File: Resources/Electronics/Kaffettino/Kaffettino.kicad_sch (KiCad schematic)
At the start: 52 parts, among them J1 PPTC101LFBN-RC, J2 OSTVN02A150, J3 OSTVN04A150, J5 OSTVN04A150, M1 RFID-RC522, U1 PCF8574AN, U2 ESP32-38Pin-Wroom, U3 DFR0299

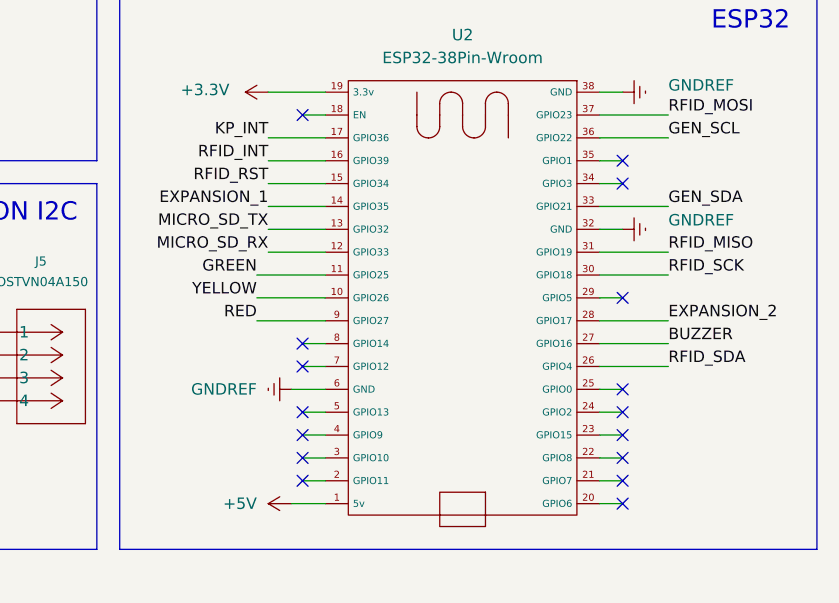
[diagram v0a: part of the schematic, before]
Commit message: NFC Reader interrupt
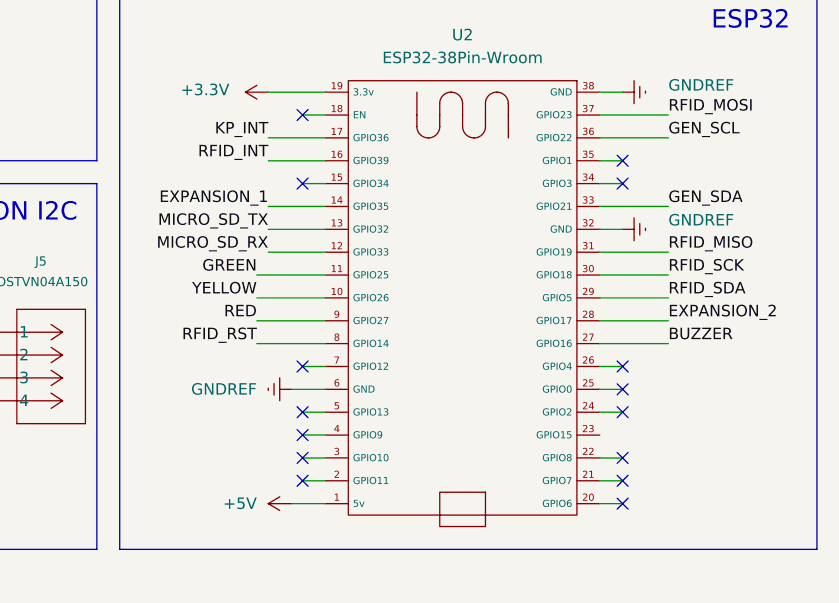
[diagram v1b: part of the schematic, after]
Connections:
- net RFID_RST: now also U2.8 (GPIO14); no longer U2.15 (GPIO34)
- net RFID_SDA: now also U2.29 (GPIO5); no longer U2.26 (GPIO4)
- no-connect marks 27 -> 26
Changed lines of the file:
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@@
+	)
+	(no_connect
+		(at 261.62 143.51)
 	)
 	(no_connect
@@
 	)
 	(no_connect
+		(at 226.06 123.19)
+	)
+	(no_connect
 		(at 219.71 67.31)
 	)
@@
 	)
 	(no_connect
-		(at 261.62 151.13)
-	)
-	(no_connect
 		(at 226.06 153.67)
 	)
@@
 	)
 	(no_connect
-		(at 226.06 140.97)
-	)
-	(no_connect
-		(at 261.62 135.89)
-	)
-	(no_connect
 		(at 226.06 156.21)
 	)
@@
 	(wire
 		(pts
-			(xy 226.06 140.97) (xy 228.6 140.97)
-		)
-		(stroke
-			(width 0)
-			(type default)
-		)
-	)
-	(wire
-		(pts
 			(xy 259.08 113.03) (xy 261.62 113.03)
 		)
@@
 	(wire
 		(pts
+			(xy 220.98 140.97) (xy 228.6 140.97)
+		)
+		(stroke
+			(width 0)
+			(type default)
+		)
+	)
+	(wire
+		(pts
 			(xy 226.06 151.13) (xy 228.6 151.13)
 		)
@@
 	(wire
 		(pts
-			(xy 261.62 135.89) (xy 259.08 135.89)
-		)
-		(stroke
-			(width 0)
-			(type default)
-		)
-	)
-	(wire
-		(pts
 			(xy 186.69 144.78) (xy 189.23 144.78)
 		)
@@
 	(wire
 		(pts
+			(xy 261.62 143.51) (xy 259.08 143.51)
+		)
+		(stroke
+			(width 0)
+			(type default)
+		)
+	)
+	(wire
+		(pts
 			(xy 77.47 20.32) (xy 82.55 20.32)
 		)
@@
 	(wire
 		(pts
+			(xy 259.08 135.89) (xy 266.7 135.89)
+		)
+		(stroke
+			(width 0)
+			(type default)
+		)
+	)
+	(wire
+		(pts
 			(xy 259.08 128.27) (xy 261.62 128.27)
 		)
@@
 	(wire
 		(pts
+			(xy 226.06 123.19) (xy 228.6 123.19)
+		)
+		(stroke
+			(width 0)
+			(type default)
+		)
+	)
+	(wire
+		(pts
 			(xy 143.51 157.48) (xy 143.51 162.56)
 		)
@@
 	(wire
 		(pts
-			(xy 259.08 143.51) (xy 266.7 143.51)
-		)
-		(stroke
-			(width 0)
-			(type default)
-		)
-	)
-	(wire
-		(pts
 			(xy 77.47 43.18) (xy 82.55 43.18)
 		)
@@
 	(wire
 		(pts
-			(xy 222.25 123.19) (xy 228.6 123.19)
-		)
-		(stroke
-			(width 0)
-			(type default)
-		)
-	)
-	(wire
-		(pts
 			(xy 115.57 27.94) (xy 115.57 33.02)
 		)
@@
 		(pts
 			(xy 95.25 114.3) (xy 95.25 71.12)
-		)
-		(stroke
-			(width 0)
-			(type default)
-		)
-	)
-	(wire
-		(pts
-			(xy 261.62 151.13) (xy 259.08 151.13)
 		)
 		(stroke
@@
 		)
 	)
+	(label "RFID_SDA"
+		(at 266.7 135.89 0)
+		(effects
+			(font
+				(size 1.27 1.27)
+			)
+			(justify left bottom)
+		)
+	)
 	(label "KP_R2"
 		(at 129.54 20.32 0)
@@
 		)
 	)
-	(label "RFID_SDA"
-		(at 266.7 143.51 0)
-		(effects
-			(font
-				(size 1.27 1.27)
-			)
-			(justify left bottom)
-		)
-	)
 	(label "KP_C2"
 		(at 129.54 71.12 0)
@@
 		)
 	)
-	(label "RFID_RST"
-		(at 222.25 123.19 180)
-		(effects
-			(font
-				(size 1.27 1.27)
-			)
-			(justify right bottom)
-		)
-	)
 	(label "MICRO_SD_TX"
 		(at 266.7 69.85 0)
@@
 		)
 	)
+	(label "RFID_RST"
+		(at 220.98 140.97 180)
+		(effects
+			(font
+				(size 1.27 1.27)
+			)
+			(justify right bottom)
+		)
+	)

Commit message: Working mp3 player, oled screen and nfc scanner
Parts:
- R24: now fitted
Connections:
- net BUZZER: now also U2.12 (GPIO33); no longer U2.27 (GPIO16)
- net EXPANSION_2: now also U2.13 (GPIO32); no longer U2.28 (GPIO17)
- net MICRO_SD_RX: now also U2.27 (GPIO16); no longer U2.12 (GPIO33)
- net MICRO_SD_TX: now also U2.28 (GPIO17); no longer U2.13 (GPIO32)
- no-connect marks 26 -> 27
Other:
- note added: "Can be used"
- note added: "MP3 PLAYER"
- note added: "NFC READER"
- note added: "OLED DISPLAY"
- note added: "STATUS LED"
- note added: "We should remember that we cannot use: - 34, 35, 36, 39: Are only input pins without an internal resistor - 6, 7, 8, 9, 10, 11: Flash memory, do not use - 0, 2: Strapping pin (booting the esp32) - 1, 3: Serial line for debugging - 4, 12, 13, 14, 25, 26, 27: Only digital reads and writes work with wifi"
- note removed: "DISPLAY OLED"
- note removed: "LED DI STATO"
- note removed: "LETTORE NFC"
- note removed: "LETTORE SD"
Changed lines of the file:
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@@
 		)
 	)
-	(text "LED DI STATO"
+	(text "STATUS LED"
 		(exclude_from_sim no)
 		(at 60.706 150.622 0)
@@
 		)
 	)
-	(text "LETTORE NFC\n"
+	(text "NFC READER\n"
 		(exclude_from_sim no)
 		(at 272.034 17.018 0)
@@
 		)
 	)
-	(text "DISPLAY OLED\n"
+	(text "Can be used"
+		(exclude_from_sim no)
+		(at 264.414 151.384 0)
+		(effects
+			(font
+				(size 1.27 1.27)
+			)
+			(justify left)
+		)
+	)
+	(text "Can be used"
+		(exclude_from_sim no)
+		(at 208.534 122.682 0)
+		(effects
+			(font
+				(size 1.27 1.27)
+			)
+			(justify left)
+		)
+	)
+	(text "We should remember that we cannot use:\n- 34, 35, 36, 39: Are only input pins without an internal resistor\n- 6, 7, 8, 9, 10, 11: Flash memory, do not use\n- 0, 2: Strapping pin (booting the esp32)\n- 1, 3: Serial line for debugging\n- 4, 12, 13, 14, 25, 26, 27: Only digital reads and writes work with wifi"
+		(exclude_from_sim no)
+		(at 302.006 126.746 0)
+		(effects
+			(font
+				(size 1.27 1.27)
+			)
+			(justify left)
+		)
+	)
+	(text "OLED DISPLAY"
 		(exclude_from_sim no)
 		(at 42.418 126.238 0)
@@
 		)
 	)
-	(text "LETTORE SD\n"
+	(text "MP3 PLAYER\n"
 		(exclude_from_sim no)
 		(at 271.78 51.816 0)
@@
 	)
 	(no_connect
-		(at 261.62 123.19)
-	)
-	(no_connect
-		(at 261.62 146.05)
+		(at 226.06 123.19)
 	)
 	(no_connect
-		(at 261.62 156.21)
+		(at 226.06 143.51)
 	)
 	(no_connect
-		(at 261.62 153.67)
+		(at 261.62 123.19)
 	)
 	(no_connect
-		(at 226.06 115.57)
+		(at 261.62 158.75)
 	)
 	(no_connect
@@
 	)
 	(no_connect
-		(at 261.62 143.51)
+		(at 261.62 151.13)
 	)
 	(no_connect
@@
 	)
 	(no_connect
-		(at 33.02 25.4)
+		(at 261.62 153.67)
 	)
 	(no_connect
-		(at 226.06 123.19)
+		(at 33.02 25.4)
 	)
 	(no_connect
@@
 	)
 	(no_connect
-		(at 226.06 143.51)
+		(at 261.62 120.65)
 	)
 	(no_connect
-		(at 226.06 151.13)
+		(at 261.62 156.21)
 	)
 	(no_connect
-		(at 261.62 148.59)
+		(at 226.06 151.13)
 	)
 	(no_connect
-		(at 226.06 153.67)
+		(at 226.06 115.57)
 	)
 	(no_connect
@@
 	)
 	(no_connect
-		(at 261.62 158.75)
+		(at 261.62 143.51)
 	)
 	(no_connect
-		(at 226.06 156.21)
+		(at 261.62 146.05)
 	)
 	(no_connect
-		(at 261.62 120.65)
+		(at 226.06 153.67)
+	)
+	(no_connect
+		(at 261.62 148.59)
+	)
+	(no_connect
+		(at 226.06 156.21)
 	)
 	(no_connect
@@
 	(wire
 		(pts
+			(xy 220.98 140.97) (xy 228.6 140.97)
+		)
+		(stroke
+			(width 0)
+			(type default)
+		)
+	)
+	(wire
+		(pts
 			(xy 115.57 101.6) (xy 115.57 106.68)
 		)
@@
 	(wire
 		(pts
-			(xy 259.08 140.97) (xy 266.7 140.97)
+			(xy 228.6 130.81) (xy 220.98 130.81)
 		)
 		(stroke
@@
 	(wire
 		(pts
-			(xy 220.98 140.97) (xy 228.6 140.97)
-		)
-		(stroke
-			(width 0)
-			(type default)
-		)
-	)
-	(wire
-		(pts
 			(xy 226.06 151.13) (xy 228.6 151.13)
 		)
@@
 	(wire
 		(pts
-			(xy 222.25 125.73) (xy 228.6 125.73)
+			(xy 220.98 125.73) (xy 228.6 125.73)
 		)
 		(stroke
@@
 	(wire
 		(pts
-			(xy 222.25 120.65) (xy 228.6 120.65)
+			(xy 220.98 120.65) (xy 228.6 120.65)
 		)
 		(stroke
@@
 	(wire
 		(pts
-			(xy 222.25 128.27) (xy 228.6 128.27)
+			(xy 265.43 138.43) (xy 259.08 138.43)
 		)
 		(stroke
@@
 	(wire
 		(pts
-			(xy 220.98 133.35) (xy 228.6 133.35)
-		)
-		(stroke
-			(width 0)
-			(type default)
-		)
-	)
-	(wire
-		(pts
 			(xy 259.08 118.11) (xy 266.7 118.11)
 		)
@@
 	(wire
 		(pts
-			(xy 222.25 130.81) (xy 228.6 130.81)
+			(xy 265.43 140.97) (xy 259.08 140.97)
 		)
 		(stroke
@@
 	(wire
 		(pts
+			(xy 220.98 135.89) (xy 228.6 135.89)
+		)
+		(stroke
+			(width 0)
+			(type default)
+		)
+	)
+	(wire
+		(pts
+			(xy 220.98 133.35) (xy 228.6 133.35)
+		)
+		(stroke
+			(width 0)
+			(type default)
+		)
+	)
+	(wire
+		(pts
 			(xy 157.48 104.14) (xy 160.02 104.14)
 		)
@@
 	(wire
 		(pts
-			(xy 255.27 64.77) (xy 252.73 64.77)
+			(xy 261.62 151.13) (xy 259.08 151.13)
 		)
 		(stroke
@@
 	(wire
 		(pts
-			(xy 261.62 153.67) (xy 259.08 153.67)
+			(xy 255.27 64.77) (xy 252.73 64.77)
 		)
 		(stroke
@@
 	(wire
 		(pts
-			(xy 233.68 22.86) (xy 250.19 22.86)
+			(xy 261.62 153.67) (xy 259.08 153.67)
 		)
 		(stroke
@@
 	(wire
 		(pts
-			(xy 69.85 71.12) (xy 78.74 71.12)
+			(xy 233.68 22.86) (xy 250.19 22.86)
 		)
 		(stroke
@@
 	(wire
 		(pts
-			(xy 95.25 63.5) (xy 95.25 20.32)
+			(xy 69.85 71.12) (xy 78.74 71.12)
 		)
 		(stroke
@@
 	(wire
 		(pts
-			(xy 226.06 148.59) (xy 228.6 148.59)
+			(xy 95.25 63.5) (xy 95.25 20.32)
 		)
 		(stroke
@@
 	(wire
 		(pts
-			(xy 261.62 120.65) (xy 259.08 120.65)
+			(xy 226.06 148.59) (xy 228.6 148.59)
 		)
 		(stroke
@@
 	(wire
 		(pts
-			(xy 220.98 138.43) (xy 228.6 138.43)
+			(xy 261.62 120.65) (xy 259.08 120.65)
 		)
 		(stroke
 			(width 0)
 			(type default)
-			(color 194 0 0 1)
 		)
 	)
@@
 	(wire
 		(pts
-			(xy 226.06 123.19) (xy 228.6 123.19)
-		)
-		(stroke
-			(width 0)
-			(type default)
-		)
-	)
-	(wire
-		(pts
 			(xy 143.51 157.48) (xy 143.51 162.56)
 		)
@@
 	(wire
 		(pts
-			(xy 220.98 135.89) (xy 228.6 135.89)
+			(xy 161.29 24.13) (xy 161.29 25.4)
 		)
 		(stroke
 			(width 0)
 			(type default)
-			(color 221 133 0 1)
 		)
 	)
 	(wire
 		(pts
-			(xy 161.29 24.13) (xy 161.29 25.4)
+			(xy 220.98 118.11) (xy 228.6 118.11)
 		)
 		(stroke
@@
 	(wire
 		(pts
-			(xy 222.25 118.11) (xy 228.6 118.11)
+			(xy 259.08 133.35) (xy 266.7 133.35)
 		)
 		(stroke
@@
 	(wire
 		(pts
-			(xy 259.08 133.35) (xy 266.7 133.35)
+			(xy 165.1 101.6) (xy 165.1 104.14)
 		)
 		(stroke
@@
 	(wire
 		(pts
-			(xy 165.1 101.6) (xy 165.1 104.14)
+			(xy 100.33 93.98) (xy 97.79 93.98)
 		)
 		(stroke
@@
 	(wire
 		(pts
-			(xy 100.33 93.98) (xy 97.79 93.98)
+			(xy 78.74 71.12) (xy 83.82 71.12)
 		)
 		(stroke
@@
 	(wire
 		(pts
-			(xy 78.74 71.12) (xy 83.82 71.12)
+			(xy 220.98 138.43) (xy 228.6 138.43)
 		)
 		(stroke
@@
 	(wire
 		(pts
+			(xy 226.06 123.19) (xy 228.6 123.19)
+		)
+		(stroke
+			(width 0)
+			(type default)
+		)
+	)
+	(wire
+		(pts
 			(xy 33.02 38.1) (xy 45.72 38.1)
 		)
@@
 	(wire
 		(pts
-			(xy 259.08 138.43) (xy 266.7 138.43)
+			(xy 228.6 128.27) (xy 220.98 128.27)
 		)
 		(stroke
@@
 	)
 	(label "BUZZER"
-		(at 266.7 140.97 0)
+		(at 220.98 130.81 180)
 		(effects
 			(font
@@
 				(color 0 0 0 1)
 			)
-			(justify left bottom)
+			(justify right bottom)
 		)
 	)
@@
 	)
 	(label "EXPANSION_1"
-		(at 222.25 125.73 180)
+		(at 220.98 125.73 180)
 		(effects
 			(font
@@
 	)
 	(label "KP_INT"
-		(at 222.25 118.11 180)
+		(at 220.98 118.11 180)
 		(effects
 			(font
@@
 	)
 	(label "EXPANSION_2"
-		(at 266.7 138.43 0)
+		(at 220.98 128.27 180)
 		(effects
 			(font
 				(size 1.27 1.27)
 			)
-			(justify left bottom)
+			(justify right bottom)
 		)
 	)
@@
 	)
 	(label "MICRO_SD_TX"
-		(at 222.25 128.27 180)
+		(at 265.43 138.43 0)
 		(effects
 			(font
 				(size 1.27 1.27)
 			)
-			(justify right bottom)
+			(justify left bottom)
 		)
 	)
@@
 	)
 	(label "RFID_INT"
-		(at 222.25 120.65 180)
+		(at 220.98 120.65 180)
 		(effects
 			(font
@@
 	)
 	(label "MICRO_SD_RX"
-		(at 222.25 130.81 180)
+		(at 265.43 140.97 0)
 		(effects
 			(font
 				(size 1.27 1.27)
 			)
-			(justify right bottom)
+			(justify left bottom)
 		)
 	)
@@
 		(in_bom yes)
 		(on_board yes)
-		(dnp yes)
+		(dnp no)
 		(property "Reference" "R24"
 			(at 219.202 35.814 0)

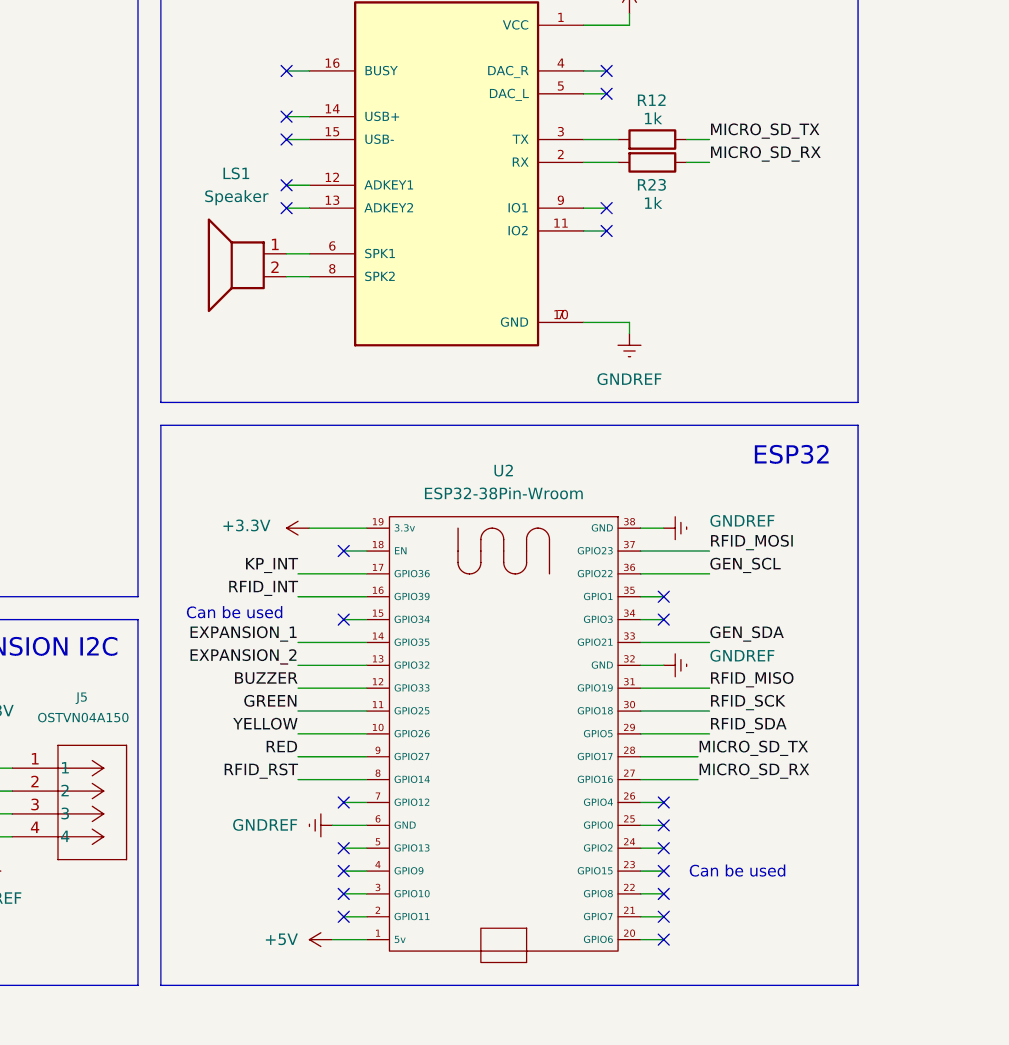
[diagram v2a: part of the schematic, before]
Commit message: Embedded: Added Buzzer and LED support
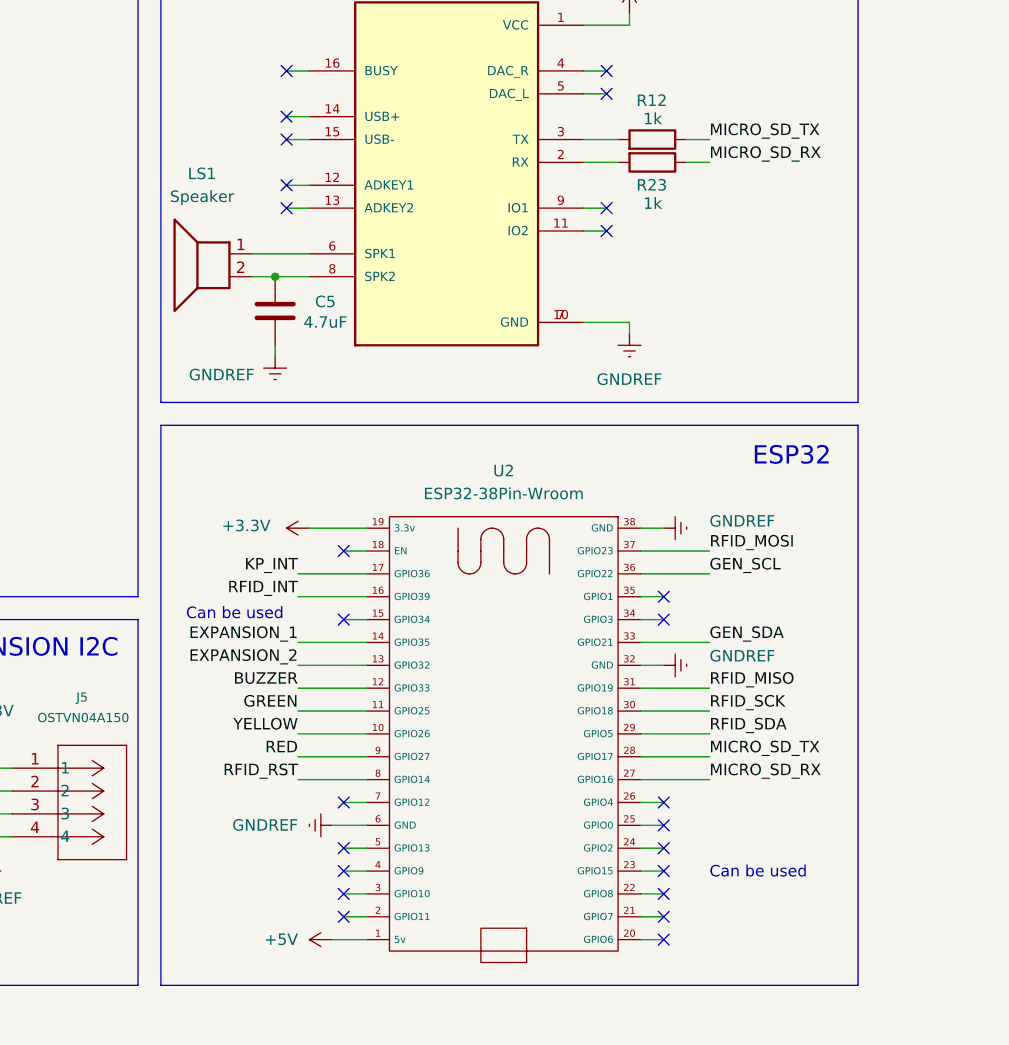
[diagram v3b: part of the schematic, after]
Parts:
- added C5: 4.7uF, Capacitor_THT:CP_Radial_D6.3mm_P2.50mm, symbol Device:C
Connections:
- net GNDREF: now also C5.2
- net at LS1.2, U3.8 (SPK2): now also C5.1
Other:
- moved on the sheet: LS1
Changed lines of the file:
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@@
 	(text "Can be used"
 		(exclude_from_sim no)
-		(at 264.414 151.384 0)
+		(at 266.7 151.384 0)
 		(effects
 			(font
@@
 	)
 	(junction
+		(at 218.44 85.09)
+		(diameter 0)
+		(color 0 0 0 0)
+	)
+	(junction
 		(at 68.58 43.18)
 		(diameter 0)
@@
 	(wire
 		(pts
+			(xy 218.44 93.98) (xy 218.44 92.71)
+		)
+		(stroke
+			(width 0)
+			(type default)
+		)
+	)
+	(wire
+		(pts
 			(xy 33.02 33.02) (xy 50.8 33.02)
 		)
@@
 	(wire
 		(pts
-			(xy 219.71 82.55) (xy 222.25 82.55)
+			(xy 215.9 82.55) (xy 222.25 82.55)
 		)
 		(stroke
@@
 	(wire
 		(pts
-			(xy 219.71 85.09) (xy 222.25 85.09)
+			(xy 215.9 85.09) (xy 218.44 85.09)
 		)
 		(stroke
@@
 	(wire
 		(pts
-			(xy 265.43 138.43) (xy 259.08 138.43)
+			(xy 266.7 138.43) (xy 259.08 138.43)
 		)
 		(stroke
@@
 	(wire
 		(pts
-			(xy 265.43 140.97) (xy 259.08 140.97)
+			(xy 266.7 140.97) (xy 259.08 140.97)
 		)
 		(stroke
@@
 	(wire
 		(pts
+			(xy 218.44 85.09) (xy 222.25 85.09)
+		)
+		(stroke
+			(width 0)
+			(type default)
+		)
+	)
+	(wire
+		(pts
 			(xy 33.02 134.62) (xy 43.18 134.62)
 		)
@@
 	)
 	(label "MICRO_SD_TX"
-		(at 265.43 138.43 0)
+		(at 266.7 138.43 0)
 		(effects
 			(font
@@
 	)
 	(label "MICRO_SD_RX"
-		(at 265.43 140.97 0)
+		(at 266.7 140.97 0)
 		(effects
 			(font
@@
 	(symbol
 		(lib_id "power:GNDREF")
+		(at 218.44 93.98 0)
+		(unit 1)
+		(exclude_from_sim no)
+		(in_bom yes)
+		(on_board yes)
+		(dnp no)
+		(property "Reference" "#PWR041"
+			(at 218.44 100.33 0)
+			(effects
+				(font
+					(size 1.27 1.27)
+				)
+				(hide yes)
+			)
+		)
+		(property "Value" "GNDREF"
+			(at 216.154 96.012 0)
+			(effects
+				(font
+					(size 1.27 1.27)
+				)
+				(justify right)
+			)
+		)
+		(property "Footprint" ""
+			(at 218.44 93.98 0)
+			(effects
+				(font
+					(size 1.27 1.27)
+				)
+				(hide yes)
+			)
+		)
+		(property "Datasheet" ""
+			(at 218.44 93.98 0)
+			(effects
+				(font
+					(size 1.27 1.27)
+				)
+				(hide yes)
+			)
+		)
+		(property "Description" "Power symbol creates a global label with name \"GNDREF\" , reference supply ground"
+			(at 218.44 93.98 0)
+			(effects
+				(font
+					(size 1.27 1.27)
+				)
+				(hide yes)
+			)
+		)
+		(pin "1"
+		)
+		(instances
+			(project "Kaffettino"
+				(path "/5e636569-7bbd-43ff-bd8f-9986b616afcc"
+					(reference "#PWR041")
+					(unit 1)
+				)
+			)
+		)
+	)
+	(symbol
+		(lib_id "power:GNDREF")
 		(at 175.26 104.14 0)
 		(unit 1)
@@
 	(symbol
 		(lib_id "Device:Speaker")
-		(at 214.63 82.55 0)
+		(at 210.82 82.55 0)
 		(mirror y)
 		(unit 1)
@@
 		(fields_autoplaced yes)
 		(property "Reference" "LS1"
-			(at 214.122 73.66 0)
+			(at 210.312 73.66 0)
 			(effects
 				(font
@@
 		)
 		(property "Value" "Speaker"
-			(at 214.122 76.2 0)
+			(at 210.312 76.2 0)
 			(effects
 				(font
@@
 		)
 		(property "Footprint" "OSTVN02A150:CONN_OSTVN02A150_OST"
-			(at 214.63 87.63 0)
+			(at 210.82 87.63 0)
 			(effects
 				(font
@@
 		)
 		(property "Datasheet" "~"
-			(at 214.884 83.82 0)
+			(at 211.074 83.82 0)
 			(effects
 				(font
@@
 		)
 		(property "Description" "Speaker"
-			(at 214.63 82.55 0)
+			(at 210.82 82.55 0)
 			(effects
 				(font
@@
 					(unit 1)
 				)
+			)
+		)
+	)
+	(symbol
+		(lib_id "Device:C")
+		(at 218.44 88.9 0)
+		(unit 1)
+		(exclude_from_sim no)
+		(in_bom yes)
+		(on_board yes)
+		(dnp no)
+		(property "Reference" "C5"
+			(at 224.028 87.884 0)
+			(effects
+				(font
+					(size 1.27 1.27)
+				)
+			)
+		)
+		(property "Value" "4.7uF"
+			(at 224.028 90.17 0)
+			(effects
+				(font
+					(size 1.27 1.27)
+				)
+			)
+		)
+		(property "Footprint" "Capacitor_THT:CP_Radial_D6.3mm_P2.50mm"
+			(at 219.4052 92.71 0)
+			(effects
+				(font
+					(size 1.27 1.27)
+				)
+				(hide yes)
+			)
+		)
+		(property "Datasheet" "~"
+			(at 218.44 88.9 0)
+			(effects
+				(font
+					(size 1.27 1.27)
+				)
+				(hide yes)
+			)
+		)
+		(property "Description" "Unpolarized capacitor"
+			(at 218.44 88.9 0)
+			(effects
+				(font
+					(size 1.27 1.27)
+				)
+				(hide yes)
+			)
+		)
+		(pin "2"
+		)
+		(pin "1"
+		)
+		(instances
+			(project "Kaffettino"
+				(path "/5e636569-7bbd-43ff-bd8f-9986b616afcc"
+					(reference "C5")
+					(unit 1)
+				)
